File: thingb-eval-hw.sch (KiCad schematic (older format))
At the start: 18 parts

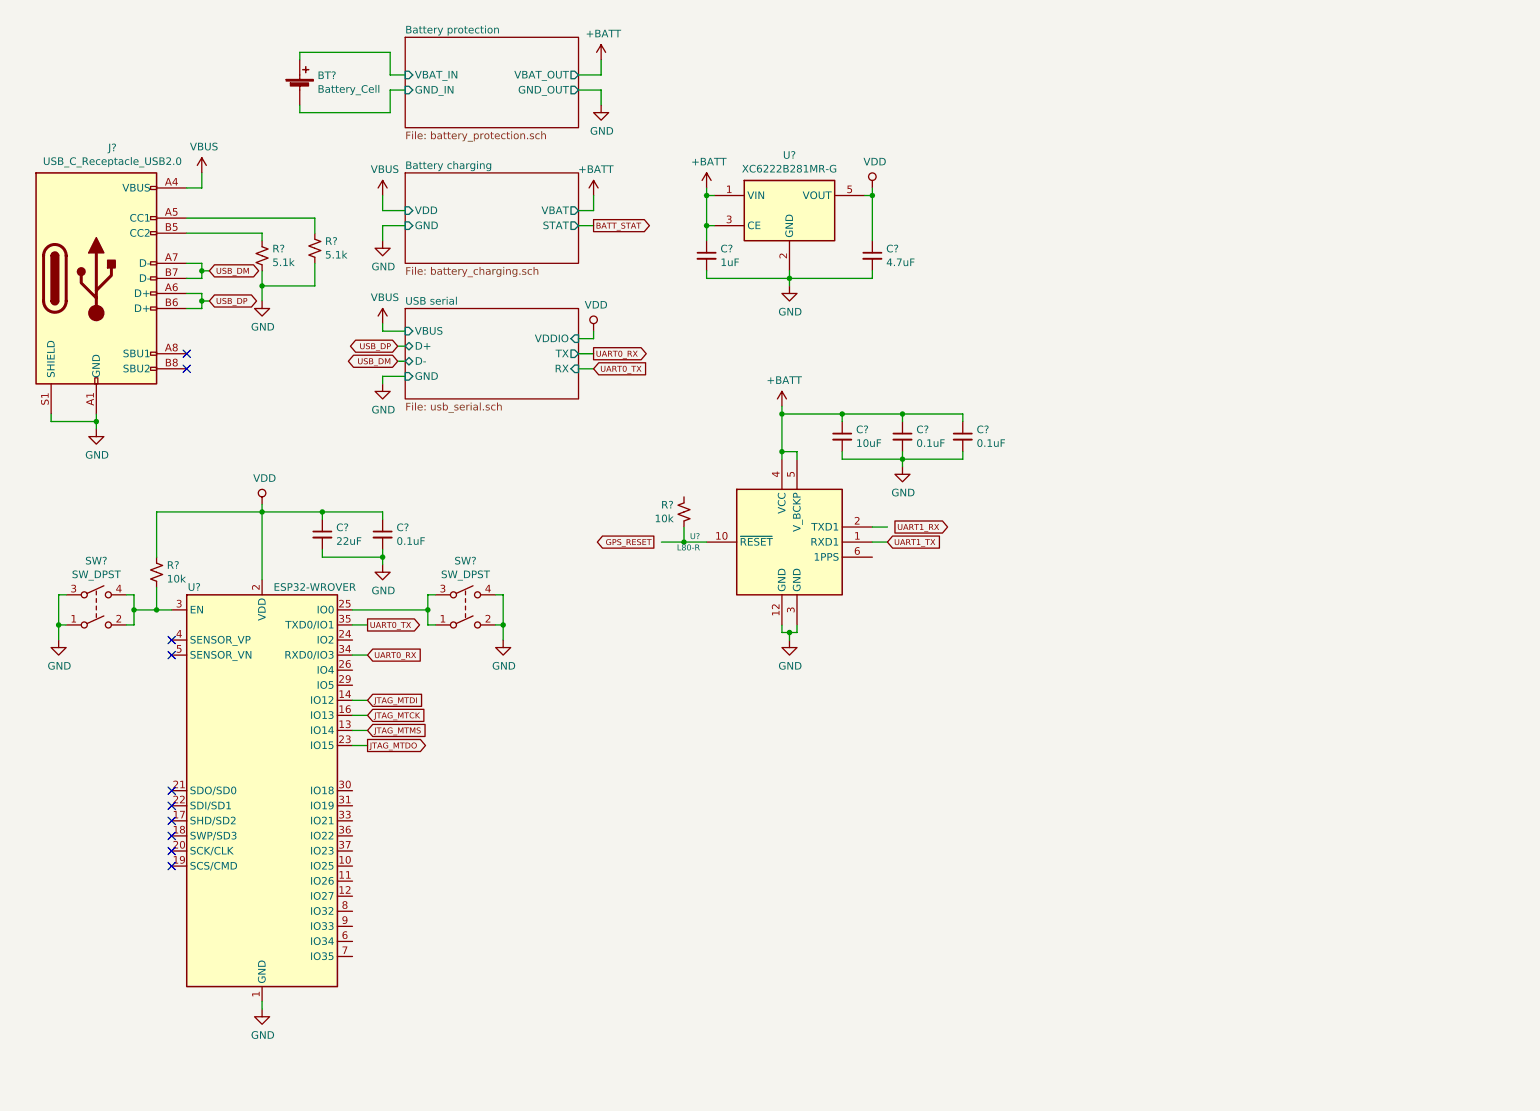
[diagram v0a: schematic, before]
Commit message: add cellular module, input, display, level shifter, and more to schematic
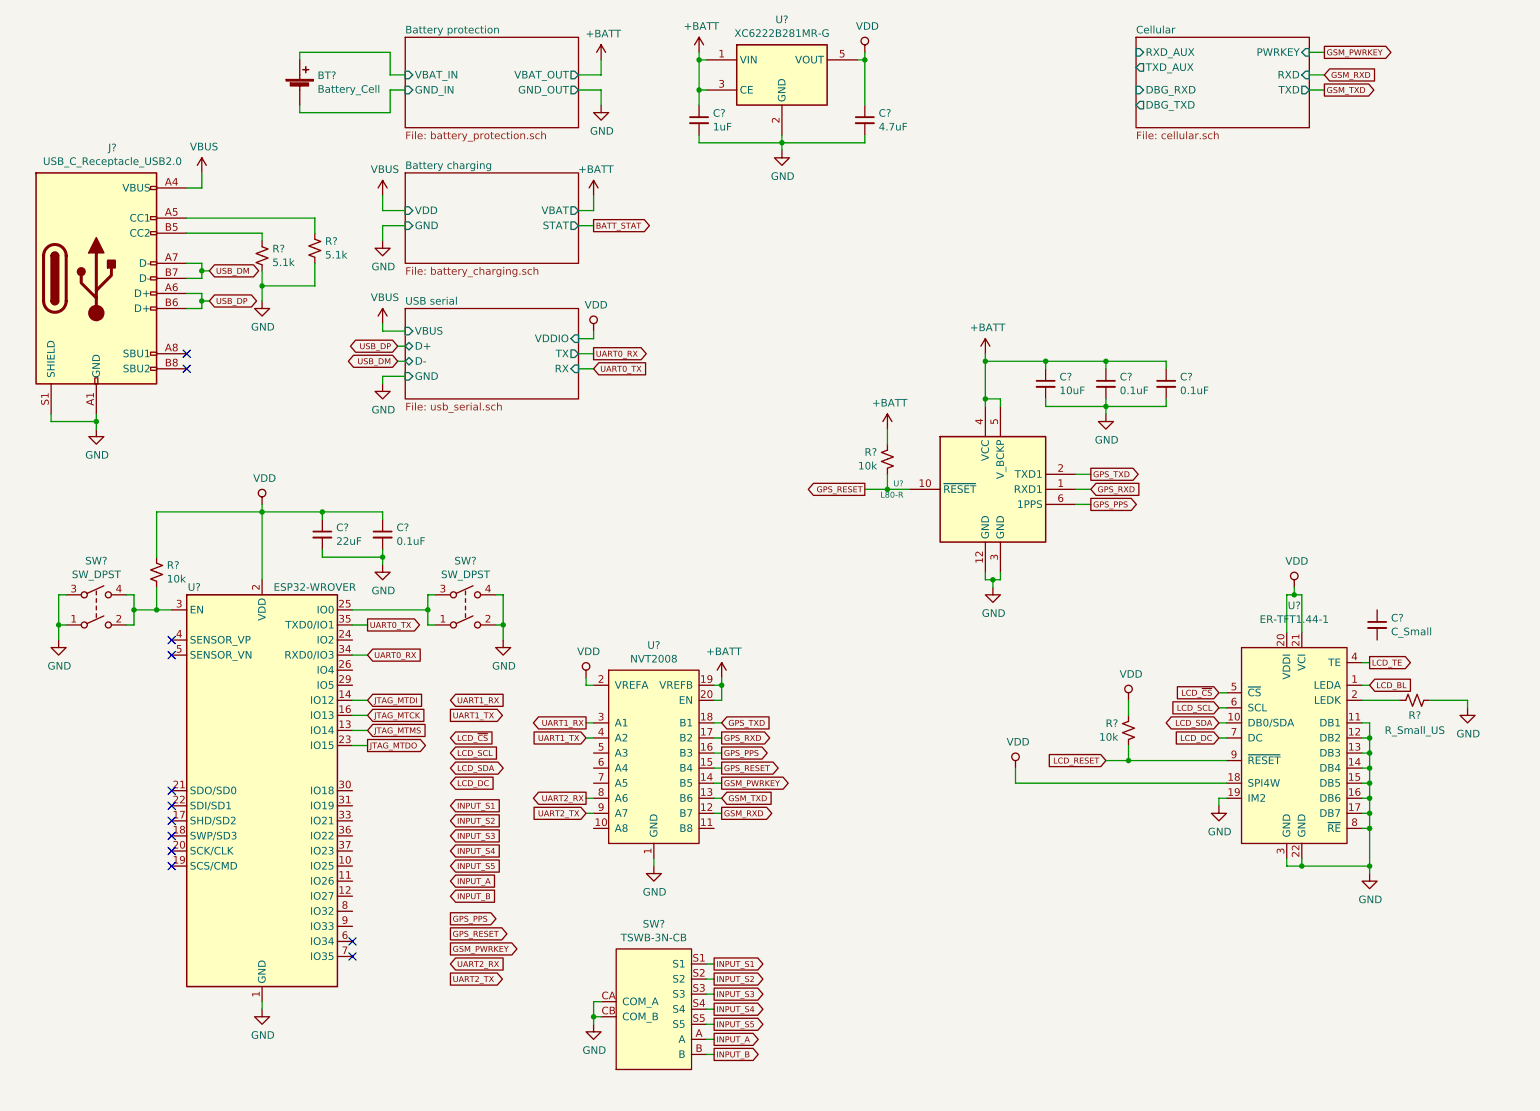
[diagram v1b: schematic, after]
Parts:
- added C?: C_Small, symbol Device:C_Small
- added R?: 10k, symbol Device:R_Small_US
- added R?: R_Small_US, symbol Device:R_Small_US
- added SW?: TSWB-3N-CB, symbol thingb:TSWB-3N-CB
- added U?: ER-TFT1.44-1, symbol thingb:ER-TFT1.44-1
- added U?: NVT2008, symbol thingb:NVT2008
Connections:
- net +BATT: now also R?.2, U?.19 (VREFB), U?.20 (EN)
- net GND: now also R?.1, SW?.CA (COM_A), SW?.CB (COM_B), U?.1 (GND), U?.11 (DB1), U?.12 (DB2), U?.13 (DB3), U?.14 (DB4), U?.15 (DB5), U?.16 (DB6), U?.17 (DB7), U?.19 (IM2), U?.22 (GND), U?.3 (GND), U?.8 (~RE)
- net GPS_RESET: now also R?.1, U?.10 (~RESET), U?.15 (B4)
- net UART1_RX: now also U?.3 (A1)
- net UART1_TX: now also U?.4 (A2); no longer U?.1 (RXD1)
- net VDD: now also R?.2, U?.18 (SPI4W), U?.2 (VREFA), U?.20 (VDDI), U?.21 (VCI)
- net GPS_TXD: now reaches U?.2 (TXD1)
- net GPS_TXD: now also U?.18 (B1)
- net GPS_PPS: now reaches U?.6 (1PPS)
- net GPS_PPS: now also U?.16 (B3)
- new net: R?.2, U?.2 (LEDK)
- new net GPS_RXD: U?.1 (RXD1), U?.17 (B2)
- new net GSM_PWRKEY: U?.14 (B5)
- new net GSM_RXD: U?.12 (B7)
- new net GSM_TXD: U?.13 (B6)
- new net INPUT_A: SW?.A
- new net INPUT_B: SW?.B
- new net INPUT_S1: SW?.S1
- new net INPUT_S2: SW?.S2
- new net INPUT_S3: SW?.S3
- new net INPUT_S4: SW?.S4
- new net INPUT_S5: SW?.S5
- new net LCD_BL: U?.1 (LEDA)
- new net LCD_DC: U?.7 (DC)
- new net LCD_RESET: R?.1, U?.9 (~RESET)
- new net LCD_SCL: U?.6 (SCL)
- new net LCD_SDA: U?.10 (DB0/SDA)
- new net LCD_TE: U?.4 (TE)
- new net LCD_~CS: U?.5 (~CS)
- new net UART2_RX: U?.8 (A6)
- new net UART2_TX: U?.9 (A7)
- no-connect marks 10 -> 12
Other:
- moved on the sheet: C?, R?, U?

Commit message: lots of improvements to schematic: fixing decoupling, matching reference designs and recommendations better, connecting pins to esp32 and adding i2c gpio expander
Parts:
- added C? (x3): 0.1uF, symbol Device:C_Small
- added J? (x2): Conn_01x04, symbol Connector_Generic:Conn_01x04
- added R? (x5): 10k, symbol Device:R_Small_US
- added U?: MCP23008_SO, Package_SO:SOIC-18W_7.5x11.6mm_P1.27mm, symbol thingb:MCP23008_SO
- C?: value C_Small -> 0.1uF
- SW? (x2): value SW_DPST -> SW_Push; symbol Switch:SW_DPST -> Switch:SW_Push
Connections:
- net Battery protection/GND_IN is gone; now on net GND: BT?.2 (-)
- net +BATT: now also C?.1, R?.1, R?.2, R?.2
- net BATT_STAT: now also U?.17 (GP7)
- net Cellular/DBG_RXD: now also J?.3 (Pin_3)
- net Cellular/DBG_TXD: now also J?.4 (Pin_4)
- net Cellular/RXD_AUX: now also J?.1 (Pin_1)
- net Cellular/TXD_AUX: now also J?.2 (Pin_2)
- net GND: now also C?.2, C?.2, C?.2, C?.2, U?.3 (A2), U?.4 (A1), U?.5 (A0), U?.9 (VSS); no longer SW?.3, SW?.4
- net GPS_PPS: now also U?.5 (SENSOR_VN); no longer U?.16 (B3)
- net GPS_RESET: now also U?.16 (B3); no longer U?.15 (B4)
- net GPS_RXD: now also R?.2
- net GSM_PWRKEY: now also U?.15 (B4), R?.1; no longer U?.14 (B5)
- net GSM_RXD: now also U?.13 (B6), R?.1; no longer U?.12 (B7)
- net GSM_TXD: now also U?.14 (B5); no longer U?.13 (B6)
- net INPUT_A: now also U?.15 (GP5)
- net INPUT_B: now also U?.16 (GP6)
- net INPUT_S1: now also U?.10 (GP0)
- net INPUT_S2: now also U?.11 (GP1)
- net INPUT_S3: now also U?.12 (GP2)
- net INPUT_S4: now also U?.13 (GP3)
- net INPUT_S5: now also U?.14 (GP4)
- net JTAG_MTCK: now also J?.2 (Pin_2)
- net JTAG_MTDI: now also J?.1 (Pin_1)
- net JTAG_MTDO: now also J?.4 (Pin_4)
- net JTAG_MTMS: now also J?.3 (Pin_3)
- net LCD_BL: now also U?.9 (IO33)
- net LCD_DC: now also U?.37 (IO23)
- net LCD_RESET: now also U?.8 (IO32)
- net LCD_SCL: now also U?.33 (IO21)
- net LCD_SDA: now also U?.36 (IO22)
- net LCD_TE: now also U?.4 (SENSOR_VP)
- net LCD_~CS: now also U?.31 (IO19)
- net UART1_RX: now also U?.6 (IO34), R?.2
- net UART1_TX: now also U?.29 (IO5)
- net UART2_RX: now also U?.7 (A5), U?.7 (IO35), R?.2; no longer U?.8 (A6)
- net UART2_TX: now also U?.30 (IO18), U?.8 (A6); no longer U?.9 (A7)
- net VDD: now also C?.1, C?.1, C?.1, R?.1, R?.1, U?.18 (VDD), U?.6 (~RESET~)
- net I2C_SCL: now reaches U?.10 (IO25)
- net I2C_SCL: now also U?.1 (SCL)
- net I2C_SDA: now reaches U?.11 (IO26)
- net I2C_SDA: now also U?.2 (SDA)
- net INPUT_INT: now reaches U?.12 (IO27)
- net INPUT_INT: now also U?.8 (INT)
- net GPIO2: now reaches U?.24 (IO2)
- net GPIO2: now also U?.5 (A3)
- net at SW?.1, U?.25 (IO0): no longer SW?.3
- net GPIO4: now reaches U?.26 (IO4)
- net GPIO4: now also U?.6 (A4)
- net at R?.2, SW?.2, U?.3 (EN): no longer SW?.4
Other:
- moved on the sheet: BT?, C?, J?, R?, SW?, U?

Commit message: annotate schematic
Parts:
- gave numbers to parts that had none: 35
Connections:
- net GND: no longer BT1.2 (-)
- new net Battery protection/GND_IN: BT1.2 (-)
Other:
- moved on the sheet: C3, C6, U3

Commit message: fix power flag things
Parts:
- renumbered C4 to C3, C3 to C4

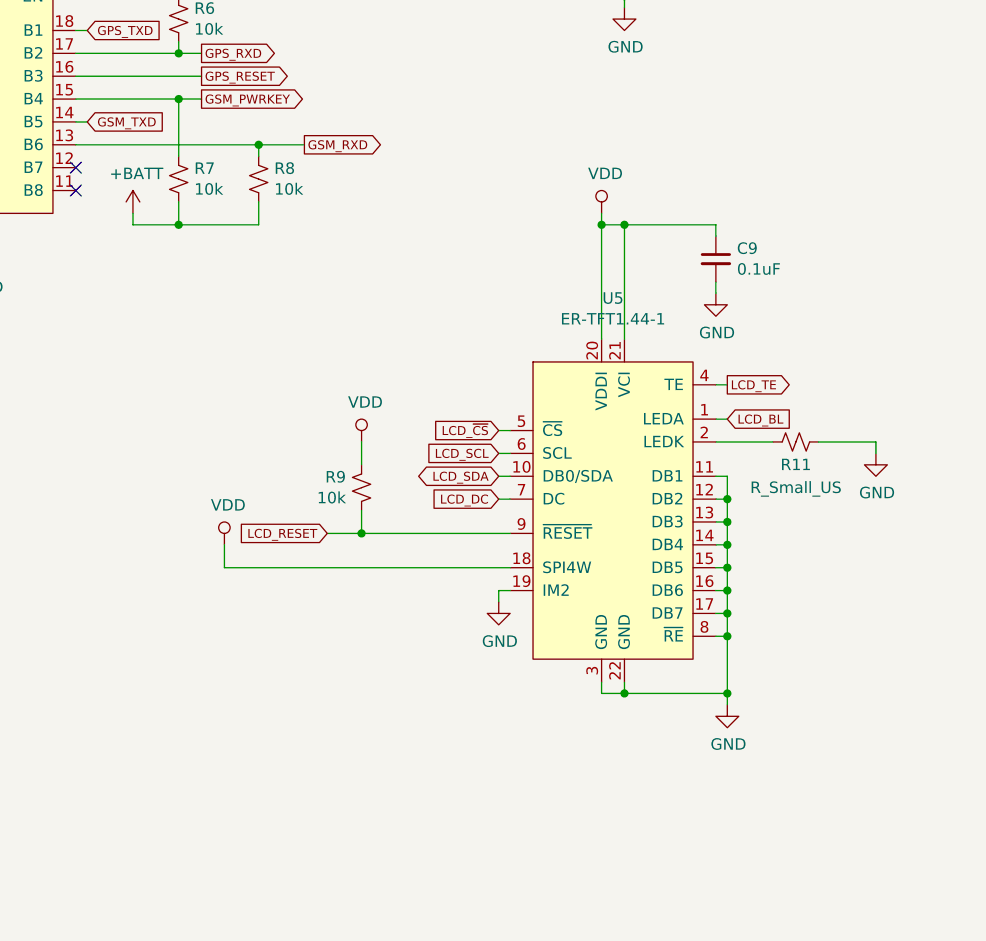
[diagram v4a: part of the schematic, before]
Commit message: add transistor to control led backlist and flip led anode and cathode positions on tft symbol
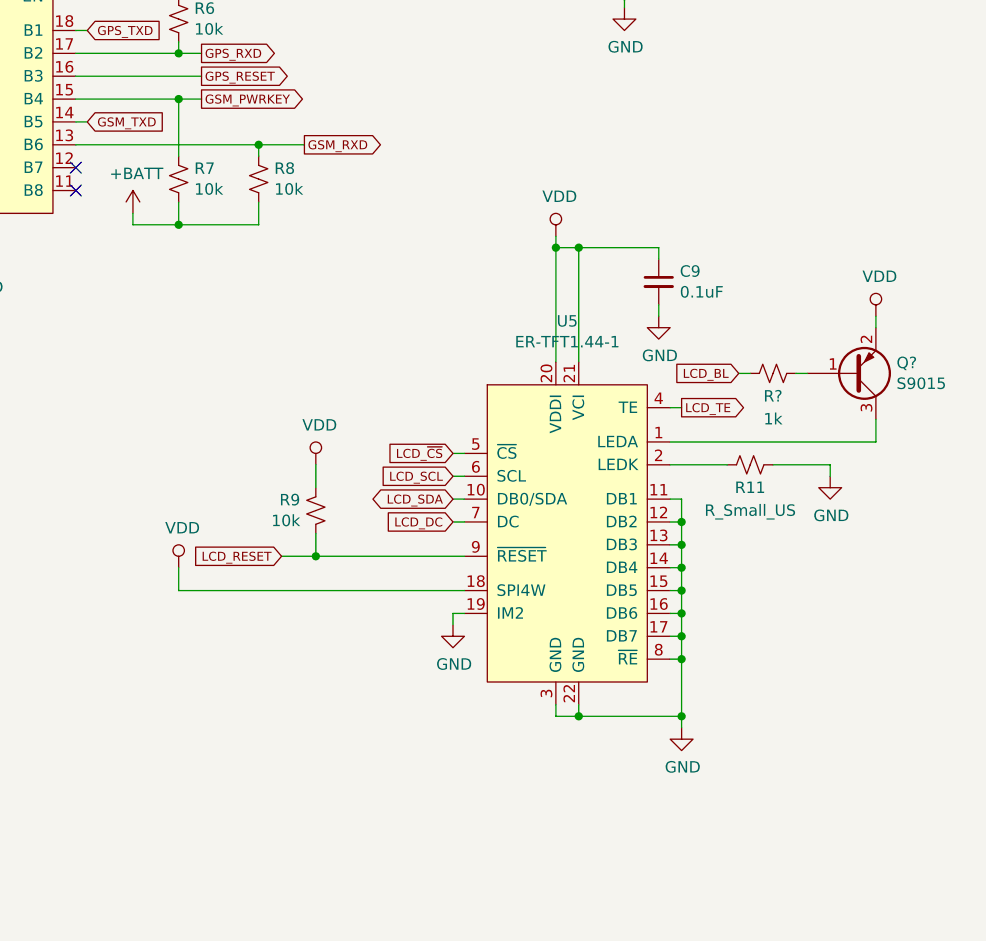
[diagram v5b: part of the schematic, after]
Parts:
- added Q?: S9015, symbol Device:Q_PNP_BEC
- added R?: 1k, symbol Device:R_Small_US
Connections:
- net LCD_BL: now also R?.2; no longer U5.1 (LEDA)
- net VDD: now also Q?.2 (E)
- new net: Q?.3 (C), U5.1 (LEDA)
- new net: Q?.1 (B), R?.1
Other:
- moved on the sheet: C9, R11, R9, U5

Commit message: reannotate schematic
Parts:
- gave numbers to parts that had none: 2
- renumbered C9 to C8, C8 to C9
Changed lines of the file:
@@
 	9050 3250 9100 3250
 $Comp
-L Device:C_Small C8
+L Device:C_Small C9
 U 1 1 5CA59CF4
 P 9400 1950
-F 0 "C8" H 9492 1996 50  0000 L CNN
+F 0 "C9" H 9492 1996 50  0000 L CNN
 F 1 "10uF" H 9492 1905 50  0000 L CNN
 F 2 "" H 9400 1950 50  0001 C CNN
@@
 	8750 6400 8750 6350
 $Comp
-L power:GND #PWR038
+L power:GND #PWR037
 U 1 1 5CA36BA3
 P 8300 6000
-F 0 "#PWR038" H 8300 5750 50  0001 C CNN
+F 0 "#PWR037" H 8300 5750 50  0001 C CNN
 F 1 "GND" H 8305 5827 50  0000 C CNN
 F 2 "" H 8300 6000 50  0001 C CNN
@@
 	7100 5850 7100 5750
 $Comp
-L Device:C_Small C9
+L Device:C_Small C8
 U 1 1 5CA51B79
 P 9200 4500
-F 0 "C9" H 9292 4546 50  0000 L CNN
+F 0 "C8" H 9292 4546 50  0000 L CNN
 F 1 "0.1uF" H 9292 4455 50  0000 L CNN
 F 2 "" H 9200 4500 50  0001 C CNN
@@
 	6650 3700 7100 3700
 $Comp
-L power:+BATT #PWR037
+L power:+BATT #PWR038
 U 1 1 5CAC81E9
 P 8350 2250
-F 0 "#PWR037" H 8350 2100 50  0001 C CNN
+F 0 "#PWR038" H 8350 2100 50  0001 C CNN
 F 1 "+BATT" H 8365 2423 50  0000 C CNN
 F 2 "" H 8350 2250 50  0001 C CNN
@@
 	9950 5300 9950 5350
 $Comp
-L power:GND #PWR?
+L power:GND #PWR045
 U 1 1 5D7A48D8
 P 9950 5350
-F 0 "#PWR?" H 9950 5100 50  0001 C CNN
+F 0 "#PWR045" H 9950 5100 50  0001 C CNN
 F 1 "GND" H 9955 5177 50  0000 C CNN
 F 2 "" H 9950 5350 50  0001 C CNN
@@
 $EndComp
 $Comp
-L power:VDD #PWR?
+L power:VDD #PWR046
 U 1 1 5D7BC7EA
 P 10150 4650
-F 0 "#PWR?" H 10150 4500 50  0001 C CNN
+F 0 "#PWR046" H 10150 4500 50  0001 C CNN
 F 1 "VDD" H 10167 4823 50  0000 C CNN
 F 2 "" H 10150 4650 50  0001 C CNN
@@
 	8850 4350 9200 4350
 $Comp
-L Device:Q_PNP_BEC Q?
+L Device:Q_PNP_BEC Q1
 U 1 1 5D7BBC33
 P 10050 4900
-F 0 "Q?" H 10240 4854 50  0000 L CNN
+F 0 "Q1" H 10240 4854 50  0000 L CNN
 F 1 "S9015" H 10240 4945 50  0000 L CNN
 F 2 "" H 10250 5000 50  0001 C CNN
@@
 $EndComp
 $Comp
-L Device:R_Small_US R?
+L Device:R_Small_US R12
 U 1 1 5D8F0B46
 P 9700 4900
-F 0 "R?" V 9800 4900 50  0000 C CNN
+F 0 "R12" V 9800 4900 50  0000 C CNN
 F 1 "1k" V 9900 4900 50  0000 C CNN
 F 2 "" H 9700 4900 50  0001 C CNN
